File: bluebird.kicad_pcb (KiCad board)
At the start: 2 copper layers, 99.8 x 99.7 mm, 90 parts, among them J1 USB_C_Receptacle_USB2.0, J2 Conn_01x02_Male, J3 Conn_01x05, J4 Conn_01x01, J5 Conn_01x01, J6 AVR-ISP-6, J7 Conn_01x04, SW1 SW_PUSH, U1 ATMEGA32U4, U2 MCP23017_SS, U3 IS31FL3731-SA, U4 PAM2401, U5 MCP73831-2-OT, Y1 FA328 16MHz

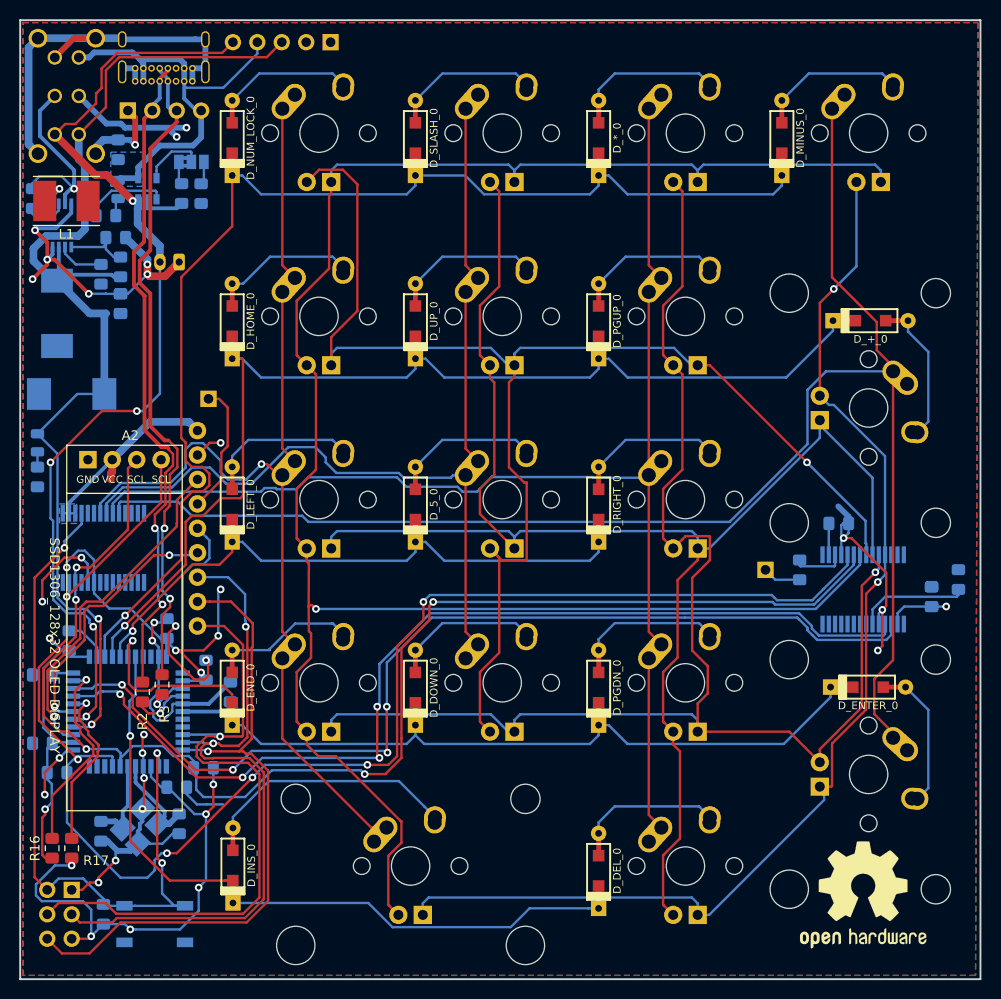
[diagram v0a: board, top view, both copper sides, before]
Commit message: Add USB C CC1/CC2 resistors, fix net overlaps.
Add labels to testpoints.
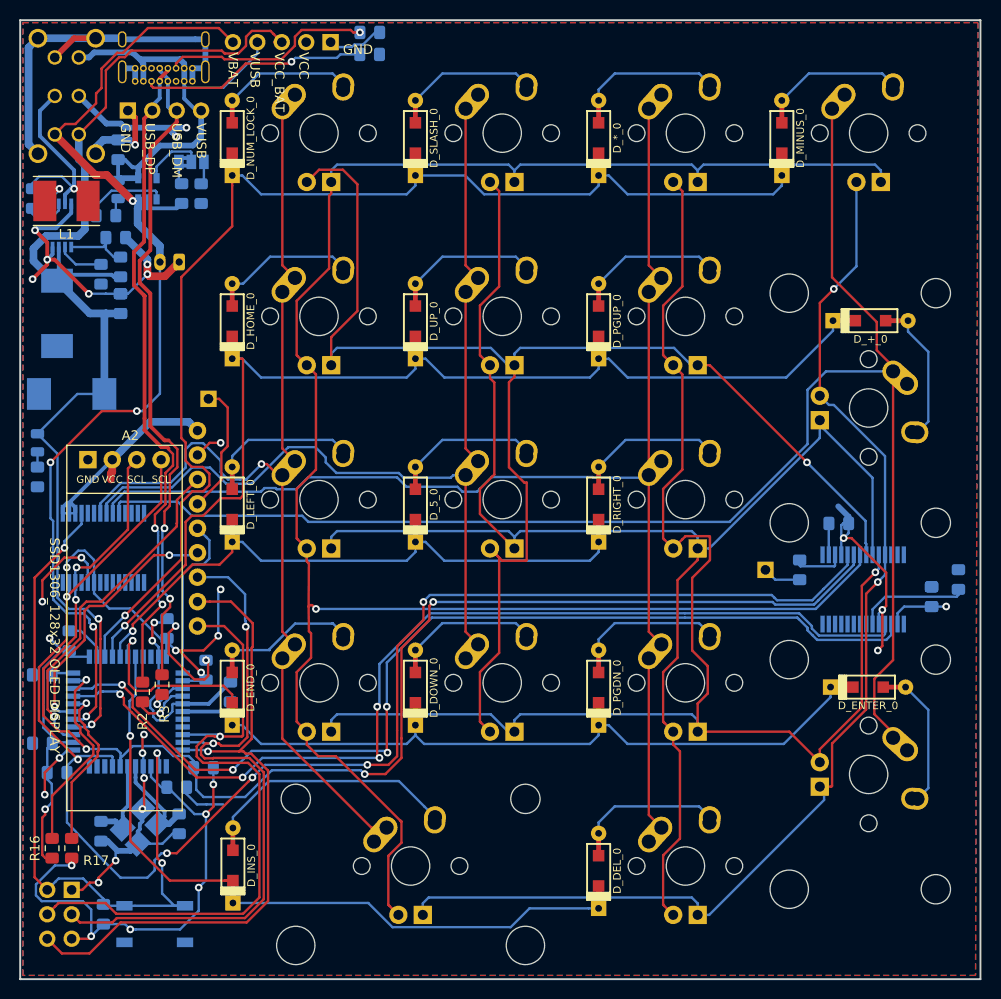
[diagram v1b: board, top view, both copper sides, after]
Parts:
- removed REF**: OSHW-Logo2_14.6x12mm_SilkScreen, Symbol:OSHW-Logo2_14.6x12mm_SilkScreen
- added R18: 5.1k, Resistor_SMD:R_0805_2012Metric_Pad1.15x1.40mm_HandSolder, B.Cu at (53.3, 22.1)
- added R19: 5.1k, Resistor_SMD:R_0805_2012Metric_Pad1.15x1.40mm_HandSolder, B.Cu at (53.3, 19.8)
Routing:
- net Net-(J1-PadA5): track 0.00 -> 23.7 mm, vias 0 -> 1
- net Net-(J1-PadB5): track 0.00 -> 22.2 mm, vias 0 -> 1
- net GND: track 209.1 -> 215.6 mm
- net VUSB: track 44.7 -> 49.3 mm
- net VCC_BAT: track 119.7 -> 124.0 mm
- net VCC: track 166.8 -> 169.7 mm
- net VBAT: track 102.4 -> 103.6 mm
- removed copper zone on B.Cu, net VCC
- removed copper zone on B.Cu, net VUSB
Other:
- board text added: "GND"
- board text added: "JLCJLCJLCJLC"
- board text added: "USB_DM"
- board text added: "USB_DP"
- board text added: "VBAT"
- board text added: "VCC"
- board text added: "VCC_BAT"
- board text added: "VUSB"
